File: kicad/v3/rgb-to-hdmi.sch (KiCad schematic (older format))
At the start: 27 parts, among them P1 CONN_02X20, P2 CONN_01X03, P3 CONN_01X06, P4 CONN_01X02, P5 CONN_01X06, P6 CONN_01X02, P7 Conn_01x01, SW1 SW_PUSH, SW2 SW_PUSH, SW3 SW_PUSH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

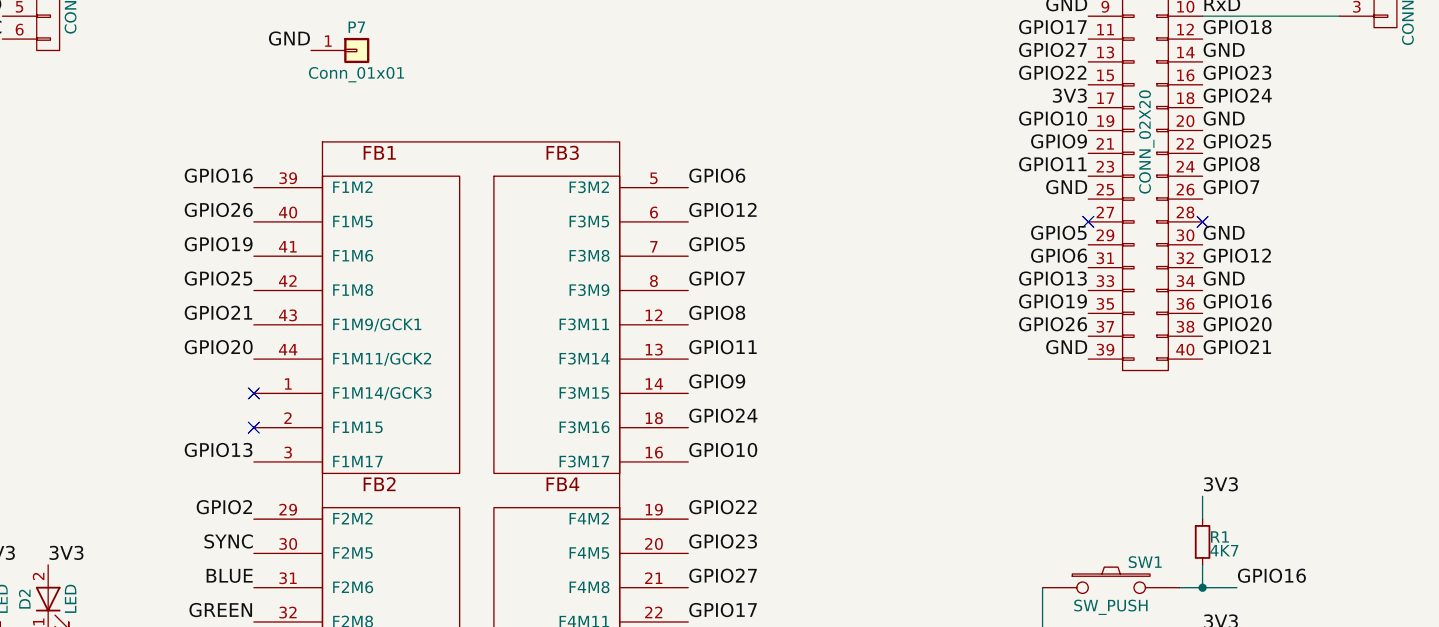
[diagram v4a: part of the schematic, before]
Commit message: KiCad: Brought gpio0/1 into use as extra cpld inputs
Change-Id: I84108de621164400689d12acfefccd9b05fdbe75
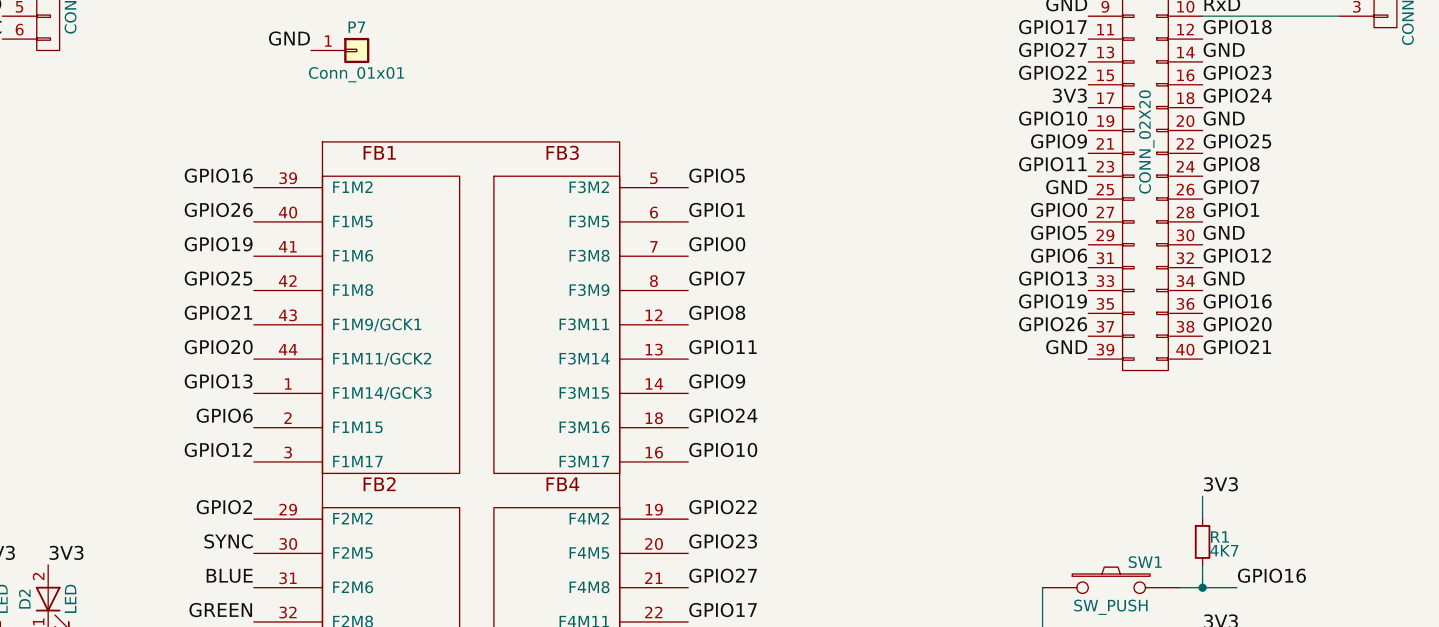
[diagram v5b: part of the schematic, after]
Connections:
- net GPIO12: now also U1.3 (F1M17); no longer U1.6 (F3M5)
- net GPIO13: now also U1.1 (F1M14/GCK3); no longer U1.3 (F1M17)
- net GPIO5: now also U1.5 (F3M2); no longer U1.7 (F3M8)
- net GPIO6: now also U1.2 (F1M15); no longer U1.5 (F3M2)
- net GPIO0: now reaches P1.27 (P27)
- net GPIO0: now also U1.7 (F3M8)
- net GPIO1: now reaches P1.28 (P28)
- net GPIO1: now also U1.6 (F3M5)
- no-connect marks 7 -> 3
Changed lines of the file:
@@
 Text Label 8950 3050 0    60   ~ 0
 GPIO21
-NoConn ~ 8450 2450
-NoConn ~ 8950 2450
 $Comp
 L CONN_01X03 P2
@@
 GPIO7
 Text Label 6700 2600 0    60   ~ 0
+GPIO0
+Text Label 6700 2450 0    60   ~ 0
+GPIO1
+Text Label 6700 2300 0    60   ~ 0
 GPIO5
-Text Label 6700 2450 0    60   ~ 0
+Text Label 4800 3500 2    60   ~ 0
 GPIO12
-Text Label 6700 2300 0    60   ~ 0
-GPIO6
-Text Label 4800 3500 2    60   ~ 0
-GPIO13
 Text Label 4800 2900 2    60   ~ 0
 GPIO21
@@
 Text Label 9100 5250 0    60   ~ 0
 GPIO19
-NoConn ~ 4800 3200
 NoConn ~ 5700 1050
 Text Label 4800 2450 2    60   ~ 0
@@
 Text Label 4800 2750 2    60   ~ 0
 GPIO25
-NoConn ~ 4800 3350
+Text Label 4800 3200 2    60   ~ 0
+GPIO13
+Text Label 4800 3350 2    60   ~ 0
+GPIO6
+Text Label 8950 2450 0    60   ~ 0
+GPIO1
+Text Label 8450 2450 2    60   ~ 0
+GPIO0
 $EndSCHEMATC

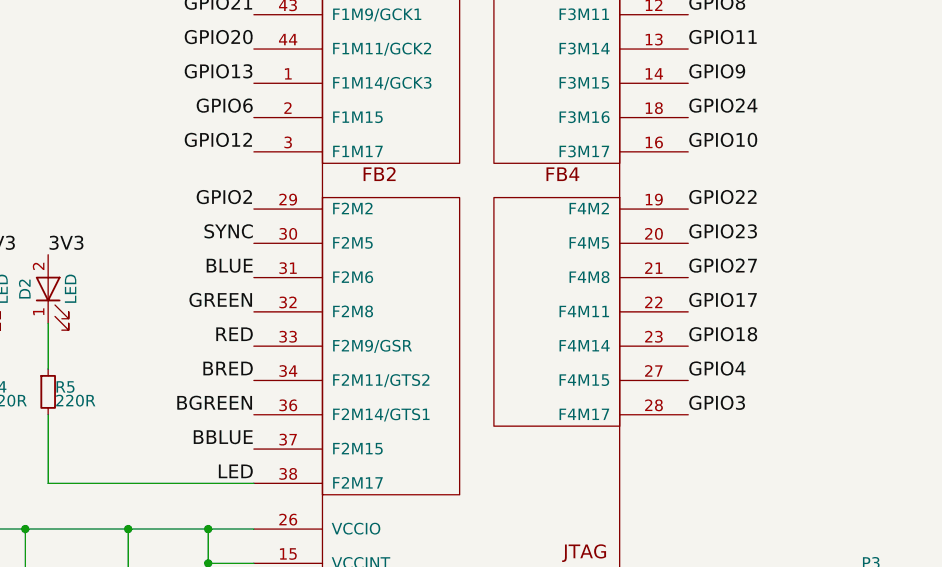
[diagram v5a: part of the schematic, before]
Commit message: KiCad: Juggled R/G/B/S inputs so GSR connects to GPIO18
Change-Id: Ib20cb67e3db2335fc415cc18dea77bd197516aa8
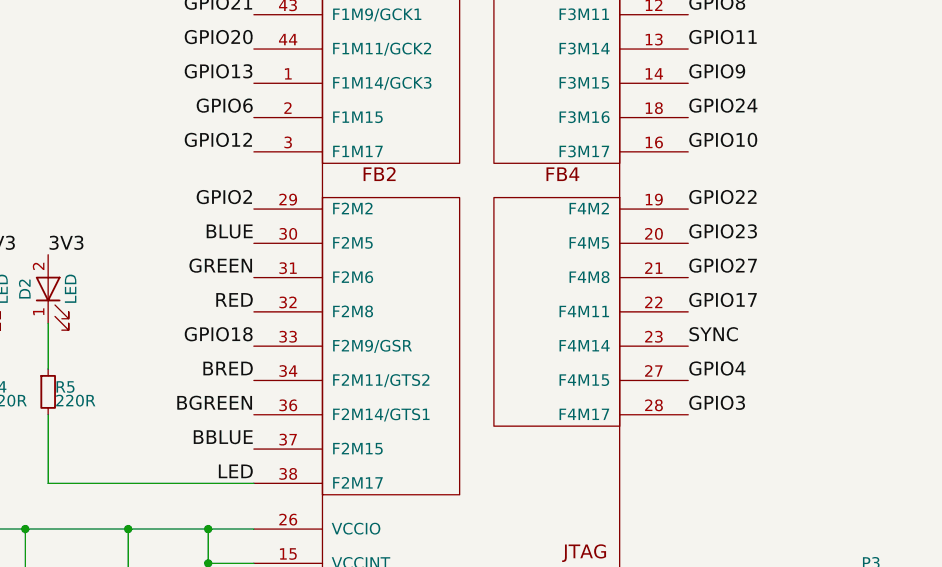
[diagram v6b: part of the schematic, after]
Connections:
- net BLUE: now also U1.30 (F2M5); no longer U1.31 (F2M6)
- net GPIO18: now also U1.33 (F2M9/GSR); no longer U1.23 (F4M14)
- net GREEN: now also U1.31 (F2M6); no longer U1.32 (F2M8)
- net RED: now also U1.32 (F2M8); no longer U1.33 (F2M9/GSR)
- net SYNC: now also U1.23 (F4M14); no longer U1.30 (F2M5)
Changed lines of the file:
@@
 GPIO4
 Text Label 6700 4350 0    60   ~ 0
-GPIO18
+SYNC
 Text Label 6700 4200 0    60   ~ 0
 GPIO17
@@
 GPIO20
 Text Label 4800 3900 2    60   ~ 0
-SYNC
+BLUE
 Text Label 4800 4050 2    60   ~ 0
-BLUE
+GREEN
 Text Label 4800 4200 2    60   ~ 0
-GREEN
+RED
 Text Label 4800 4350 2    60   ~ 0
-RED
+GPIO18
 NoConn ~ -500 3250
 $Comp

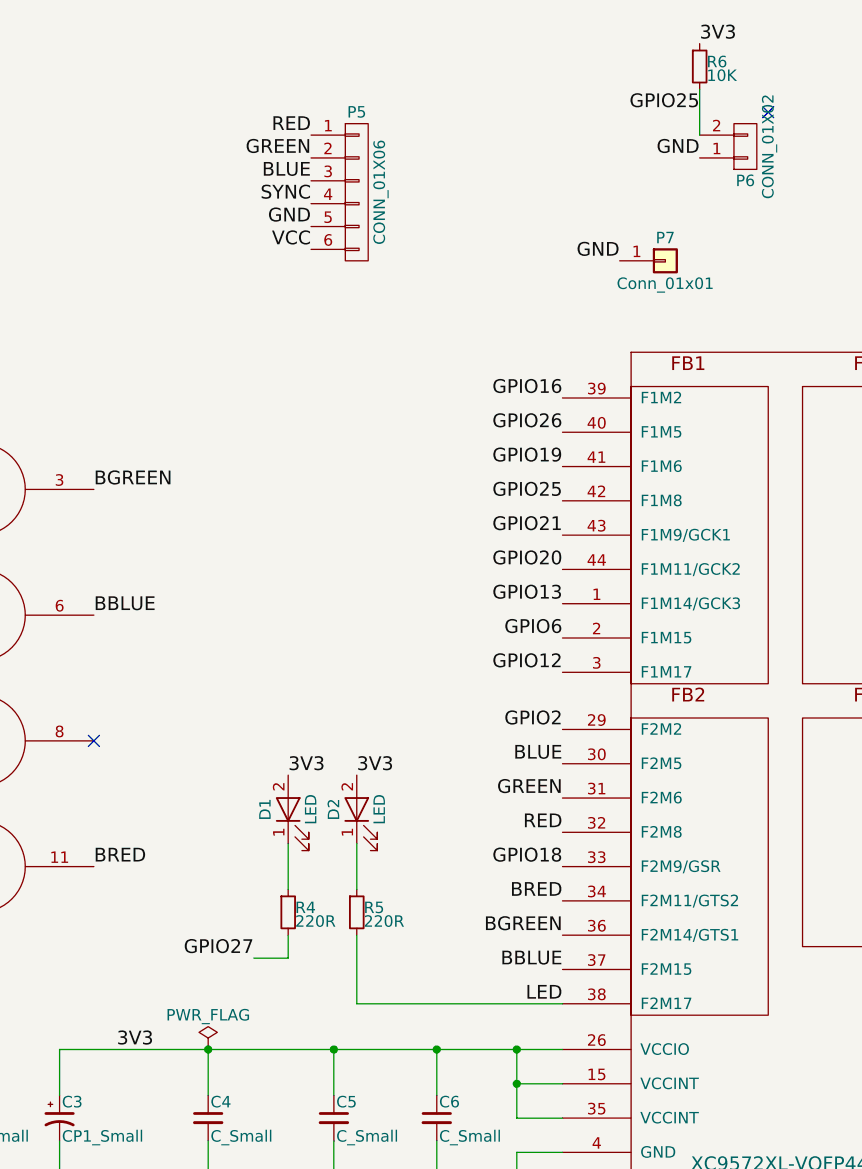
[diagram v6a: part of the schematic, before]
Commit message: KiCad: Final set of CPLD pinout changes
Change-Id: Ic3bbec75507d185d1a1419b75b4cf4d1f649dc78
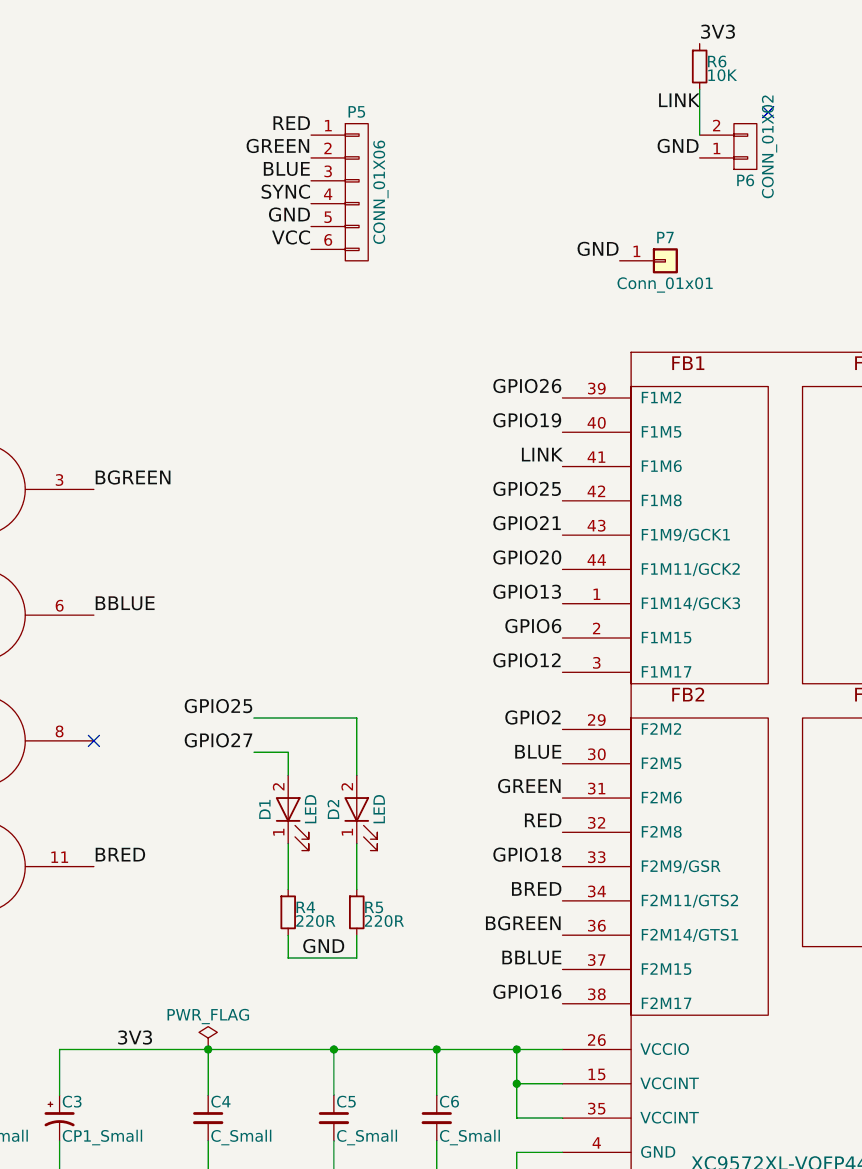
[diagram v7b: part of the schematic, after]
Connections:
- net 3V3: no longer D1.2 (A), D2.2 (A)
- net GND: now also R4.2, R5.2
- net GPIO16: now also U1.38 (F2M17); no longer U1.39 (F1M2)
- net GPIO19: now also U1.40 (F1M5); no longer U1.41 (F1M6)
- net GPIO25: now also D2.2 (A); no longer P6.2 (P2), R6.2
- net GPIO26: now also U1.39 (F1M2); no longer U1.40 (F1M5)
- net GPIO27: now also D1.2 (A); no longer R4.2
- removed net LED: R5.2, U1.38 (F2M17)
- new net LINK: P6.2 (P2), R6.2, U1.41 (F1M6)
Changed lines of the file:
@@
 $EndComp
 Text Label 4800 2300 2    60   ~ 0
-GPIO16
+GPIO26
 Text Label 8450 1750 2    60   ~ 0
 GPIO27
@@
 	1    0    0    -1
 $EndComp
-Wire Wire Line
-	4800 4950 3900 4950
-Wire Wire Line
-	3900 4950 3900 4650
 $Comp
 L LED D2
@@
 Wire Wire Line
 	3900 4250 3900 4450
-Text Label 3900 3950 0    60   ~ 0
-3V3
 $Comp
 L LED D1
@@
 	1    0    0    -1
 $EndComp
-Text Label 3600 3950 0    60   ~ 0
-3V3
 Wire Wire Line
 	3600 4250 3600 4450
 Wire Wire Line
 	3600 4650 3600 4750
-Wire Wire Line
-	3600 4750 3450 4750
-Text Label 3450 4750 2    60   ~ 0
+Text Label 3450 3850 2    60   ~ 0
 GPIO27
-Text Label 4800 4950 2    60   ~ 0
-LED
 $Comp
 L CONN_01X02 P6
@@
 Text Label 5400 1250 2    60   ~ 0
 GND
-Text Label 5400 1050 2    60   ~ 0
-GPIO25
 Text Label 8950 2150 0    60   ~ 0
 GPIO25
@@
 NoConn ~ 5700 1050
 Text Label 4800 2450 2    60   ~ 0
-GPIO26
+GPIO19
 Text Label 4800 2600 2    60   ~ 0
-GPIO19
+LINK
 Text Label 4800 2750 2    60   ~ 0
 GPIO25
@@
 Text Label 8450 2450 2    60   ~ 0
 GPIO0
+Text Label 3450 3700 2    60   ~ 0
+GPIO25
+Wire Wire Line
+	3600 3950 3600 3850
+Wire Wire Line
+	3600 3850 3450 3850
+Wire Wire Line
+	3900 3950 3900 3700
+Wire Wire Line
+	3900 3700 3450 3700
+Wire Wire Line
+	3900 4650 3900 4750
+Wire Wire Line
+	3900 4750 3600 4750
+Text Label 3850 4750 2    60   ~ 0
+GND
+Text Label 5400 1050 2    60   ~ 0
+LINK
+Text Label 4800 4950 2    60   ~ 0
+GPIO16
 $EndSCHEMATC
